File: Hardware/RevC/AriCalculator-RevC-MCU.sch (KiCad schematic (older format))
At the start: 13 parts, among them CON1 BDM, CON2 SPI, IC1 MC9S12G

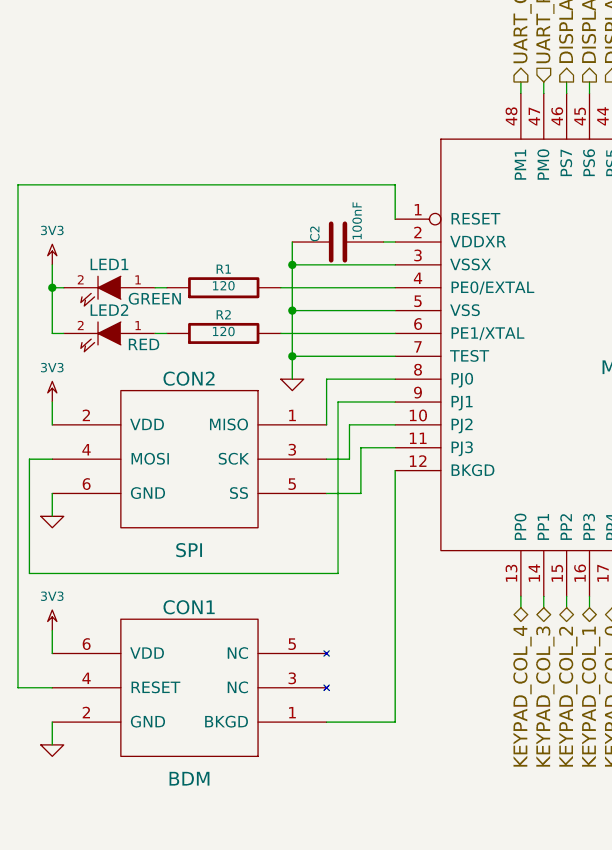
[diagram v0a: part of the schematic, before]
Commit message: cleaned up schematic
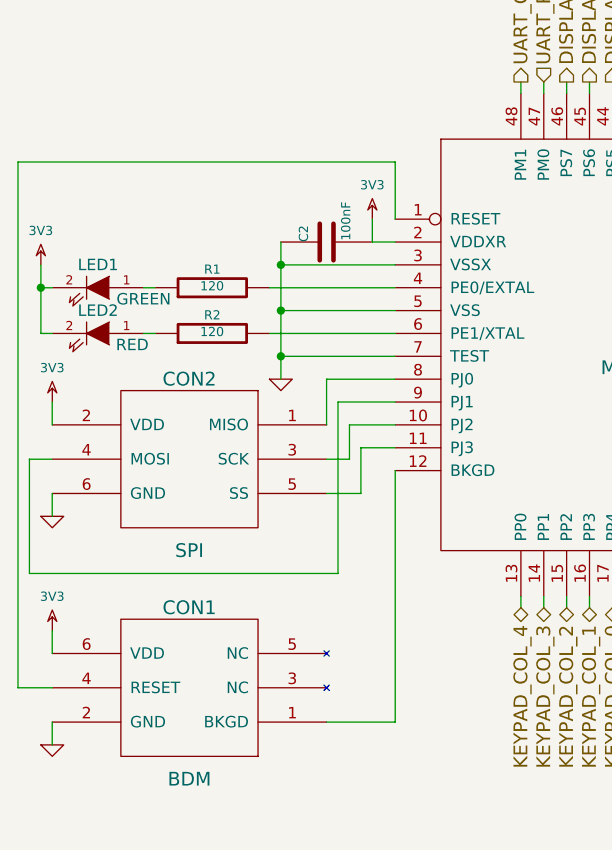
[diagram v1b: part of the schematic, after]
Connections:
- net 3V3: now also C2.2, IC1.2 (VDDXR)
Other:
- moved on the sheet: C2, LED1, LED2, R1, R2
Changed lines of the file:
@@
 $EndComp
 $Comp
-L 3V3 #PWR32
+L 3V3 #PWR33
 U 1 1 544FF35F
 P 4450 1300
-F 0 "#PWR32" H 4450 1400 40  0001 C CNN
+F 0 "#PWR33" H 4450 1400 40  0001 C CNN
 F 1 "3V3" H 4450 1449 40  0000 C CNN
 F 2 "" H 4450 1300 60  0000 C CNN
@@
 L C C2
 U 1 1 544FF3C3
-P 2550 2000
-F 0 "C2" H 2550 2100 40  0000 L CNN
-F 1 "100nF" H 2556 1915 40  0000 L CNN
-F 2 "~" H 2588 1850 30  0000 C CNN
-F 3 "~" H 2550 2000 60  0000 C CNN
-	1    2550 2000
+P 2500 2000
+F 0 "C2" H 2500 2100 40  0000 L CNN
+F 1 "100nF" H 2506 1915 40  0000 L CNN
+F 2 "~" H 2538 1850 30  0000 C CNN
+F 3 "~" H 2500 2000 60  0000 C CNN
+	1    2500 2000
 	0    -1   -1   0
 $EndComp
@@
 L GND #PWR025
 U 1 1 544FF410
-P 2350 2600
-F 0 "#PWR025" H 2350 2600 30  0001 C CNN
-F 1 "GND" H 2350 2530 30  0001 C CNN
-F 2 "" H 2350 2600 60  0000 C CNN
-F 3 "" H 2350 2600 60  0000 C CNN
-	1    2350 2600
+P 2300 2600
+F 0 "#PWR025" H 2300 2600 30  0001 C CNN
+F 1 "GND" H 2300 2530 30  0001 C CNN
+F 2 "" H 2300 2600 60  0000 C CNN
+F 3 "" H 2300 2600 60  0000 C CNN
+	1    2300 2600
 	1    0    0    -1
 $EndComp
@@
 L R R1
 U 1 1 544FF846
-P 2050 2200
-F 0 "R1" V 2130 2200 40  0000 C CNN
-F 1 "120" V 2057 2201 40  0000 C CNN
-F 2 "~" V 1980 2200 30  0000 C CNN
-F 3 "~" H 2050 2200 30  0000 C CNN
-	1    2050 2200
+P 2000 2200
+F 0 "R1" V 2080 2200 40  0000 C CNN
+F 1 "120" V 2007 2201 40  0000 C CNN
+F 2 "~" V 1930 2200 30  0000 C CNN
+F 3 "~" H 2000 2200 30  0000 C CNN
+	1    2000 2200
 	0    -1   -1   0
 $EndComp
@@
 L R R2
 U 1 1 544FF855
-P 2050 2400
-F 0 "R2" V 2130 2400 40  0000 C CNN
-F 1 "120" V 2057 2401 40  0000 C CNN
-F 2 "~" V 1980 2400 30  0000 C CNN
-F 3 "~" H 2050 2400 30  0000 C CNN
-	1    2050 2400
+P 2000 2400
+F 0 "R2" V 2080 2400 40  0000 C CNN
+F 1 "120" V 2007 2401 40  0000 C CNN
+F 2 "~" V 1930 2400 30  0000 C CNN
+F 3 "~" H 2000 2400 30  0000 C CNN
+	1    2000 2400
 	0    -1   -1   0
 $EndComp
@@
 L LED LED1
 U 1 1 544FF88C
-P 1550 2200
-F 0 "LED1" H 1550 2300 50  0000 C CNN
-F 1 "GREEN" H 1350 2150 50  0000 C CNN
-F 2 "~" H 1550 2200 60  0000 C CNN
-F 3 "~" H 1550 2200 60  0000 C CNN
-	1    1550 2200
+P 1500 2200
+F 0 "LED1" H 1500 2300 50  0000 C CNN
+F 1 "GREEN" H 1300 2150 50  0000 C CNN
+F 2 "~" H 1500 2200 60  0000 C CNN
+F 3 "~" H 1500 2200 60  0000 C CNN
+	1    1500 2200
 	-1   0    0    -1
 $EndComp
@@
 L LED LED2
 U 1 1 544FF89B
-P 1550 2400
-F 0 "LED2" H 1550 2500 50  0000 C CNN
-F 1 "RED" H 1400 2350 50  0000 C CNN
-F 2 "~" H 1550 2400 60  0000 C CNN
-F 3 "~" H 1550 2400 60  0000 C CNN
-	1    1550 2400
+P 1500 2400
+F 0 "LED2" H 1500 2500 50  0000 C CNN
+F 1 "RED" H 1350 2350 50  0000 C CNN
+F 2 "~" H 1500 2400 60  0000 C CNN
+F 3 "~" H 1500 2400 60  0000 C CNN
+	1    1500 2400
 	-1   0    0    -1
 $EndComp
@@
 L 3V3 #PWR26
 U 1 1 544FF8D2
-P 1300 2100
-F 0 "#PWR26" H 1300 2200 40  0001 C CNN
-F 1 "3V3" H 1300 2249 40  0000 C CNN
-F 2 "" H 1300 2100 60  0000 C CNN
-F 3 "" H 1300 2100 60  0000 C CNN
-	1    1300 2100
+P 1250 2100
+F 0 "#PWR26" H 1250 2200 40  0001 C CNN
+F 1 "3V3" H 1250 2249 40  0000 C CNN
+F 2 "" H 1250 2100 60  0000 C CNN
+F 3 "" H 1250 2100 60  0000 C CNN
+	1    1250 2100
 	1    0    0    -1
 $EndComp
@@
 DISPLAY_BACKLIGHT
 Wire Wire Line
-	2800 2000 2750 2000
-Wire Wire Line
-	2800 2100 2350 2100
-Wire Wire Line
-	2350 2000 2350 2600
-Wire Wire Line
-	2350 2300 2800 2300
-Connection ~ 2350 2100
-Wire Wire Line
-	2350 2500 2800 2500
-Connection ~ 2350 2300
-Connection ~ 2350 2500
+	2800 2000 2700 2000
+Wire Wire Line
+	2800 2100 2300 2100
+Wire Wire Line
+	2300 2000 2300 2600
+Wire Wire Line
+	2300 2300 2800 2300
+Connection ~ 2300 2100
+Wire Wire Line
+	2300 2500 2800 2500
+Connection ~ 2300 2300
+Connection ~ 2300 2500
 Wire Wire Line
 	1300 4100 1300 4200
@@
 	1300 3950 1150 3950
 Wire Wire Line
-	1150 3950 1150 1750
-Wire Wire Line
-	1150 1750 2800 1750
-Wire Wire Line
-	2800 1750 2800 1900
-Wire Wire Line
-	2800 2200 2300 2200
-Wire Wire Line
-	2800 2400 2300 2400
-Wire Wire Line
-	1800 2200 1750 2200
-Wire Wire Line
-	1800 2400 1750 2400
-Wire Wire Line
-	1350 2200 1300 2200
-Wire Wire Line
-	1300 2100 1300 2400
-Wire Wire Line
-	1300 2400 1350 2400
-Connection ~ 1300 2200
+	1150 3950 1150 1650
+Wire Wire Line
+	1150 1650 2800 1650
+Wire Wire Line
+	2800 1650 2800 1900
+Wire Wire Line
+	2800 2200 2250 2200
+Wire Wire Line
+	2800 2400 2250 2400
+Wire Wire Line
+	1750 2200 1700 2200
+Wire Wire Line
+	1750 2400 1700 2400
+Wire Wire Line
+	1300 2200 1250 2200
+Wire Wire Line
+	1250 2100 1250 2400
+Wire Wire Line
+	1250 2400 1300 2400
+Connection ~ 1250 2200
 Wire Wire Line
 	5000 3000 5050 3000
@@
 Wire Wire Line
 	5000 1900 6000 1900
+$Comp
+L 3V3 #PWR32
+U 1 1 5450CFC7
+P 2700 1900
+F 0 "#PWR32" H 2700 2000 40  0001 C CNN
+F 1 "3V3" H 2700 2049 40  0000 C CNN
+F 2 "" H 2700 1900 60  0000 C CNN
+F 3 "" H 2700 1900 60  0000 C CNN
+	1    2700 1900
+	1    0    0    -1
+$EndComp
+Wire Wire Line
+	2700 2000 2700 1900
 $EndSCHEMATC

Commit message: work in progress
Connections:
- net +BATT: now also IC1.26 (PAD8); no longer IC1.25 (PAD0)
- net KEYPAD_COL_0: now also IC1.18 (PP5); no longer IC1.17 (PP4)
- net KEYPAD_COL_1: now also IC1.17 (PP4); no longer IC1.16 (PP3)
- net KEYPAD_COL_2: now also IC1.16 (PP3); no longer IC1.15 (PP2)
- net KEYPAD_COL_3: now also IC1.15 (PP2); no longer IC1.14 (PP1)
- net KEYPAD_COL_4: now also IC1.14 (PP1); no longer IC1.13 (PP0)
- net KEYPAD_ROW_A: now also IC1.25 (PAD0); no longer IC1.27 (PAD1)
- net KEYPAD_ROW_B: now also IC1.27 (PAD1); no longer IC1.29 (PAD2)
- net KEYPAD_ROW_C: now also IC1.29 (PAD2); no longer IC1.31 (PAD3)
- net KEYPAD_ROW_D: now also IC1.31 (PAD3); no longer IC1.33 (PAD4)
- net KEYPAD_ROW_E: now also IC1.33 (PAD4); no longer IC1.34 (PAD5)
- net KEYPAD_ROW_F: now also IC1.34 (PAD5); no longer IC1.35 (PAD6)
- net at IC1.28 (PAD9): now also R5.2, R6.1
- new net KEYPAD_COL_5: IC1.13 (PP0)
- new net KEYPAD_ROW_G: IC1.35 (PAD6)
- now unconnected: IC1.36 (PAD7)
- no-connect marks 10 -> 8
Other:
- moved on the sheet: R5, R6
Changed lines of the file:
@@
 Sheet 6 6
 Title "MCU"
-Date "3 nov 2014"
+Date "4 nov 2014"
 Rev "RevC"
 Comp "Dirk Heisswolf"
@@
 L VUSB #PWR028
 U 1 1 54500312
-P 6000 1300
-F 0 "#PWR028" H 6000 1250 20  0001 C CNN
-F 1 "VUSB" H 6000 1400 30  0000 C CNN
-F 2 "" H 6000 1300 60  0000 C CNN
-F 3 "" H 6000 1300 60  0000 C CNN
-	1    6000 1300
+P 6000 2100
+F 0 "#PWR028" H 6000 2050 20  0001 C CNN
+F 1 "VUSB" H 6000 2200 30  0000 C CNN
+F 2 "" H 6000 2100 60  0000 C CNN
+F 3 "" H 6000 2100 60  0000 C CNN
+	1    6000 2100
 	1    0    0    -1
 $EndComp
@@
 L R R5
 U 1 1 54500321
-P 6000 1600
-F 0 "R5" V 6080 1600 40  0000 C CNN
-F 1 "8K2" V 6007 1601 40  0000 C CNN
-F 2 "~" V 5930 1600 30  0000 C CNN
-F 3 "~" H 6000 1600 30  0000 C CNN
-	1    6000 1600
+P 6000 2400
+F 0 "R5" V 6080 2400 40  0000 C CNN
+F 1 "8K2" V 6007 2401 40  0000 C CNN
+F 2 "~" V 5930 2400 30  0000 C CNN
+F 3 "~" H 6000 2400 30  0000 C CNN
+	1    6000 2400
 	-1   0    0    -1
 $EndComp
@@
 L R R6
 U 1 1 54500330
-P 6000 2200
-F 0 "R6" V 6080 2200 40  0000 C CNN
-F 1 "10K" V 6007 2201 40  0000 C CNN
-F 2 "~" V 5930 2200 30  0000 C CNN
-F 3 "~" H 6000 2200 30  0000 C CNN
-	1    6000 2200
+P 6000 3000
+F 0 "R6" V 6080 3000 40  0000 C CNN
+F 1 "10K" V 6007 3001 40  0000 C CNN
+F 2 "~" V 5930 3000 30  0000 C CNN
+F 3 "~" H 6000 3000 30  0000 C CNN
+	1    6000 3000
 	-1   0    0    -1
 $EndComp
@@
 L GND #PWR029
 U 1 1 5450033F
-P 6000 2500
-F 0 "#PWR029" H 6000 2500 30  0001 C CNN
-F 1 "GND" H 6000 2430 30  0001 C CNN
-F 2 "" H 6000 2500 60  0000 C CNN
-F 3 "" H 6000 2500 60  0000 C CNN
-	1    6000 2500
+P 6000 3300
+F 0 "#PWR029" H 6000 3300 30  0001 C CNN
+F 1 "GND" H 6000 3230 30  0001 C CNN
+F 2 "" H 6000 3300 60  0000 C CNN
+F 3 "" H 6000 3300 60  0000 C CNN
+	1    6000 3300
 	1    0    0    -1
 $EndComp
@@
 Connection ~ 1250 2200
 Wire Wire Line
-	5000 3000 5050 3000
-Wire Wire Line
-	6000 1300 6000 1350
-Wire Wire Line
-	6000 1850 6000 1950
-Connection ~ 6000 1900
-Wire Wire Line
-	6000 2450 6000 2500
+	6000 2100 6000 2150
+Wire Wire Line
+	6000 2650 6000 2750
+Connection ~ 6000 2700
+Wire Wire Line
+	6000 3250 6000 3300
 Wire Wire Line
 	4450 3550 4450 3800
@@
 NoConn ~ 4150 3550
 NoConn ~ 4050 3550
-NoConn ~ 3850 3550
-NoConn ~ 5000 2900
 NoConn ~ 5000 2500
-NoConn ~ 5000 2700
 NoConn ~ 5000 2300
 NoConn ~ 4050 1350
+Text HLabel 3850 3600 3    60   3State ~ 0
+KEYPAD_COL_0
 Text HLabel 3750 3600 3    60   3State ~ 0
-KEYPAD_COL_0
+KEYPAD_COL_1
 Text HLabel 3650 3600 3    60   3State ~ 0
-KEYPAD_COL_1
+KEYPAD_COL_2
 Text HLabel 3550 3600 3    60   3State ~ 0
-KEYPAD_COL_2
+KEYPAD_COL_3
 Text HLabel 3450 3600 3    60   3State ~ 0
-KEYPAD_COL_3
-Text HLabel 3350 3600 3    60   3State ~ 0
 KEYPAD_COL_4
+Text HLabel 5050 3000 2    60   Input ~ 0
+KEYPAD_ROW_A
 Text HLabel 5050 2800 2    60   Input ~ 0
-KEYPAD_ROW_A
+KEYPAD_ROW_B
 Text HLabel 5050 2600 2    60   Input ~ 0
-KEYPAD_ROW_B
+KEYPAD_ROW_C
 Text HLabel 5050 2400 2    60   Input ~ 0
-KEYPAD_ROW_C
+KEYPAD_ROW_D
 Text HLabel 5050 2200 2    60   Input ~ 0
-KEYPAD_ROW_D
+KEYPAD_ROW_E
 Text HLabel 5050 2100 2    60   Input ~ 0
-KEYPAD_ROW_E
-Text HLabel 5050 2000 2    60   Input ~ 0
 KEYPAD_ROW_F
 $Comp
 L +BATT #PWR030
 U 1 1 544FFB66
-P 5050 3000
-F 0 "#PWR030" H 5050 2950 20  0001 C CNN
-F 1 "+BATT" H 5050 3100 30  0000 C CNN
-F 2 "" H 5050 3000 60  0000 C CNN
-F 3 "" H 5050 3000 60  0000 C CNN
-	1    5050 3000
+P 5050 2900
+F 0 "#PWR030" H 5050 2850 20  0001 C CNN
+F 1 "+BATT" V 5050 3050 30  0000 C CNN
+F 2 "" H 5050 2900 60  0000 C CNN
+F 3 "" H 5050 2900 60  0000 C CNN
+	1    5050 2900
 	0    1    1    0
 $EndComp
 Wire Wire Line
-	3350 3550 3350 3600
-Wire Wire Line
 	3450 3550 3450 3600
 Wire Wire Line
@@
 Wire Wire Line
 	3750 3550 3750 3600
+Wire Wire Line
+	3850 3550 3850 3600
 Wire Wire Line
 	5000 2800 5050 2800
@@
 Wire Wire Line
 	4300 1000 6150 1000
-Wire Wire Line
-	5000 1900 6000 1900
 $Comp
 L 3V3 #PWR32
@@
 Wire Wire Line
 	2700 2000 2700 1900
+Text HLabel 3350 3600 3    60   BiDi ~ 0
+KEYPAD_COL_5
+Wire Wire Line
+	3350 3600 3350 3550
+Wire Wire Line
+	5050 3000 5000 3000
+Text HLabel 5050 2000 2    60   Input ~ 0
+KEYPAD_ROW_G
+NoConn ~ 5000 1900
+Wire Wire Line
+	5050 2900 5000 2900
+Wire Wire Line
+	5000 2700 6000 2700
 $EndSCHEMATC
